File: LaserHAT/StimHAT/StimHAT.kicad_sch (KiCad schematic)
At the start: 112 parts, among them J1 GPIO, J10 OLED 0.91 (GND VCC SCL SDA), J101 ELECTRODE E1/E2, J102 B4B-PH-K-S(LF)(SN), J103 5V TO DC-DC POD, J5 GT-USB-7010ASV, J6 BNC TRIGGER IN, J7 BNC STIM OUT, Q3 AP30P30Q, Q4 DMMT5401, Q5 AP30P30Q, SW10 MSK12C02, SW6 TS-1088-AR02016, SW7 SKRHADE010, SW9 TS-1088-AR02016, U1 M24C32-WDW6TP, U101 ISO7741FDBQR, U104 TLV76050DBZR, U105 DAC60501ZDGSR, U106 OPA2192IDGKR, U107 CD74HC4053PWR, U108 DG418DY-T1-E3, U109 ISO1640BDR, U110 TLV1702AIDGKR, U4 MCP1700T-3302E/MB, U5 AP2171W, U6 CH340N, U7 MSPM0G1507SRHBR, U8 74LVC2G17GW

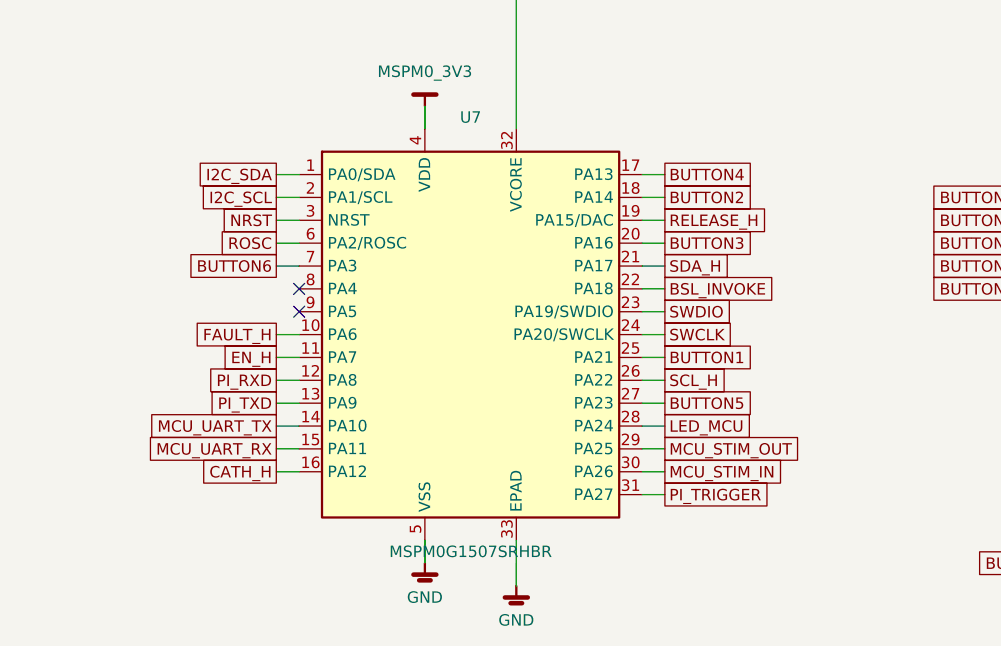
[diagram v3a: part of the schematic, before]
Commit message: StimHAT: MCU pin map re-optimised for the placement (isolator lines east on TIMA0 CCP3/CCP1/FAULT0 + ADC0 ch3/ch2, buttons and LED west/south, STIM_IN on TIMG8_CCP0); schematic, board and README updated
Co-Authored-By: Claude Fable 5.1 <noreply@anthropic.com>
Claude-Session: https://claude.ai/code/session_015kiXLxnPpBaXdXJu2EMvn7
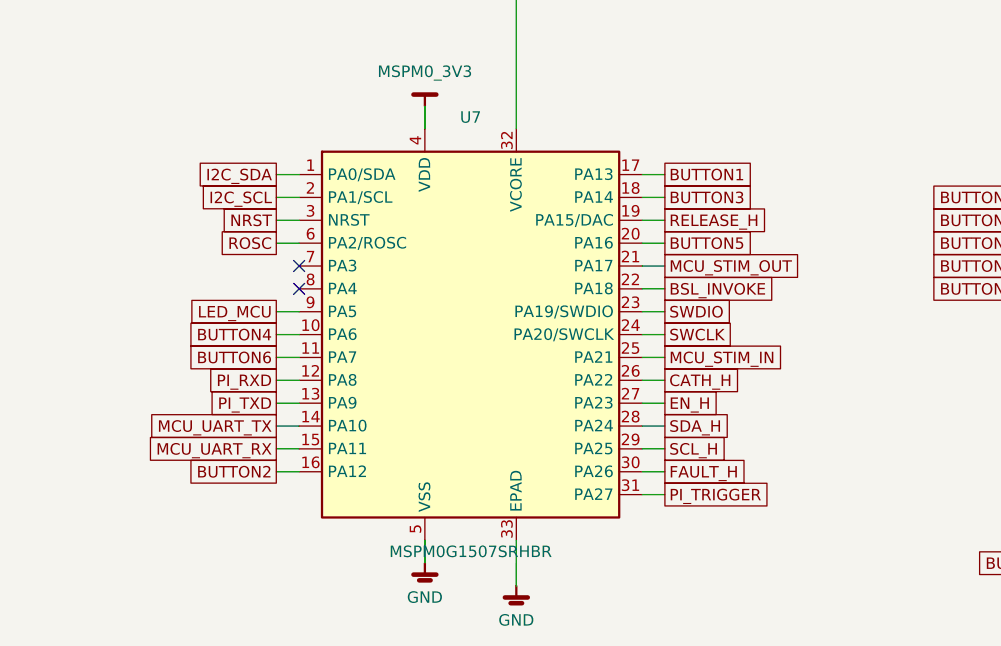
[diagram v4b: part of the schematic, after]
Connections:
- net BUTTON1: now also U7.17 (PA13); no longer U7.25 (PA21)
- net BUTTON2: now also U7.16 (PA12); no longer U7.18 (PA14)
- net BUTTON3: now also U7.18 (PA14); no longer U7.20 (PA16)
- net BUTTON4: now also U7.10 (PA6); no longer U7.17 (PA13)
- net BUTTON5: now also U7.20 (PA16); no longer U7.27 (PA23)
- net BUTTON6: now also U7.11 (PA7); no longer U7.7 (PA3)
- net CATH_H: now also U7.26 (PA22); no longer U7.16 (PA12)
- net EN_H: now also U7.27 (PA23); no longer U7.11 (PA7)
- net FAULT_H: now also U7.30 (PA26); no longer U7.10 (PA6)
- net LED_MCU: now also U7.9 (PA5); no longer U7.28 (PA24)
- net MCU_STIM_IN: now also U7.25 (PA21); no longer U7.30 (PA26)
- net MCU_STIM_OUT: now also U7.21 (PA17); no longer U7.29 (PA25)
- net SCL_H: now also U7.29 (PA25); no longer U7.26 (PA22)
- net SDA_H: now also U7.28 (PA24); no longer U7.21 (PA17)
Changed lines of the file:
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@@
   (global_label "ROSC" (shape passive) (at 364.49 71.12 180) (fields_autoplaced yes) (effects (font (size 1.27 1.27)) (justify right))
     (property "Intersheetrefs" "${INTERSHEET_REFS}" (at 364.49 71.12 0) (effects (font (size 1.27 1.27)) (hide yes))))
-  (global_label "BUTTON6" (shape passive) (at 364.49 73.66 180) (fields_autoplaced yes) (effects (font (size 1.27 1.27)) (justify right))
-    (property "Intersheetrefs" "${INTERSHEET_REFS}" (at 364.49 73.66 0) (effects (font (size 1.27 1.27)) (hide yes))))
-  (global_label "FAULT_H" (shape passive) (at 364.49 81.28 180) (fields_autoplaced yes) (effects (font (size 1.27 1.27)) (justify right))
+  (global_label "LED_MCU" (shape passive) (at 364.49 78.74 180) (fields_autoplaced yes) (effects (font (size 1.27 1.27)) (justify right))
+    (property "Intersheetrefs" "${INTERSHEET_REFS}" (at 364.49 78.74 0) (effects (font (size 1.27 1.27)) (hide yes))))
+  (global_label "BUTTON4" (shape passive) (at 364.49 81.28 180) (fields_autoplaced yes) (effects (font (size 1.27 1.27)) (justify right))
     (property "Intersheetrefs" "${INTERSHEET_REFS}" (at 364.49 81.28 0) (effects (font (size 1.27 1.27)) (hide yes))))
-  (global_label "EN_H" (shape passive) (at 364.49 83.82 180) (fields_autoplaced yes) (effects (font (size 1.27 1.27)) (justify right))
+  (global_label "BUTTON6" (shape passive) (at 364.49 83.82 180) (fields_autoplaced yes) (effects (font (size 1.27 1.27)) (justify right))
     (property "Intersheetrefs" "${INTERSHEET_REFS}" (at 364.49 83.82 0) (effects (font (size 1.27 1.27)) (hide yes))))
   (global_label "PI_RXD" (shape passive) (at 364.49 86.36 180) (fields_autoplaced yes) (effects (font (size 1.27 1.27)) (justify right))
@@
   (global_label "MCU_UART_RX" (shape passive) (at 364.49 93.98 180) (fields_autoplaced yes) (effects (font (size 1.27 1.27)) (justify right))
     (property "Intersheetrefs" "${INTERSHEET_REFS}" (at 364.49 93.98 0) (effects (font (size 1.27 1.27)) (hide yes))))
-  (global_label "CATH_H" (shape passive) (at 364.49 96.52 180) (fields_autoplaced yes) (effects (font (size 1.27 1.27)) (justify right))
+  (global_label "BUTTON2" (shape passive) (at 364.49 96.52 180) (fields_autoplaced yes) (effects (font (size 1.27 1.27)) (justify right))
     (property "Intersheetrefs" "${INTERSHEET_REFS}" (at 364.49 96.52 0) (effects (font (size 1.27 1.27)) (hide yes))))
-  (global_label "BUTTON4" (shape passive) (at 407.67 63.5 0) (fields_autoplaced yes) (effects (font (size 1.27 1.27)) (justify left))
+  (global_label "BUTTON1" (shape passive) (at 407.67 63.5 0) (fields_autoplaced yes) (effects (font (size 1.27 1.27)) (justify left))
     (property "Intersheetrefs" "${INTERSHEET_REFS}" (at 407.67 63.5 0) (effects (font (size 1.27 1.27)) (hide yes))))
-  (global_label "BUTTON2" (shape passive) (at 407.67 66.04 0) (fields_autoplaced yes) (effects (font (size 1.27 1.27)) (justify left))
+  (global_label "BUTTON3" (shape passive) (at 407.67 66.04 0) (fields_autoplaced yes) (effects (font (size 1.27 1.27)) (justify left))
     (property "Intersheetrefs" "${INTERSHEET_REFS}" (at 407.67 66.04 0) (effects (font (size 1.27 1.27)) (hide yes))))
   (global_label "RELEASE_H" (shape passive) (at 407.67 68.58 0) (fields_autoplaced yes) (effects (font (size 1.27 1.27)) (justify left))
     (property "Intersheetrefs" "${INTERSHEET_REFS}" (at 407.67 68.58 0) (effects (font (size 1.27 1.27)) (hide yes))))
-  (global_label "BUTTON3" (shape passive) (at 407.67 71.12 0) (fields_autoplaced yes) (effects (font (size 1.27 1.27)) (justify left))
+  (global_label "BUTTON5" (shape passive) (at 407.67 71.12 0) (fields_autoplaced yes) (effects (font (size 1.27 1.27)) (justify left))
     (property "Intersheetrefs" "${INTERSHEET_REFS}" (at 407.67 71.12 0) (effects (font (size 1.27 1.27)) (hide yes))))
-  (global_label "SDA_H" (shape passive) (at 407.67 73.66 0) (fields_autoplaced yes) (effects (font (size 1.27 1.27)) (justify left))
+  (global_label "MCU_STIM_OUT" (shape passive) (at 407.67 73.66 0) (fields_autoplaced yes) (effects (font (size 1.27 1.27)) (justify left))
     (property "Intersheetrefs" "${INTERSHEET_REFS}" (at 407.67 73.66 0) (effects (font (size 1.27 1.27)) (hide yes))))
   (global_label "BSL_INVOKE" (shape passive) (at 407.67 76.2 0) (fields_autoplaced yes) (effects (font (size 1.27 1.27)) (justify left))
@@
   (global_label "SWCLK" (shape passive) (at 407.67 81.28 0) (fields_autoplaced yes) (effects (font (size 1.27 1.27)) (justify left))
     (property "Intersheetrefs" "${INTERSHEET_REFS}" (at 407.67 81.28 0) (effects (font (size 1.27 1.27)) (hide yes))))
-  (global_label "BUTTON1" (shape passive) (at 407.67 83.82 0) (fields_autoplaced yes) (effects (font (size 1.27 1.27)) (justify left))
+  (global_label "MCU_STIM_IN" (shape passive) (at 407.67 83.82 0) (fields_autoplaced yes) (effects (font (size 1.27 1.27)) (justify left))
     (property "Intersheetrefs" "${INTERSHEET_REFS}" (at 407.67 83.82 0) (effects (font (size 1.27 1.27)) (hide yes))))
-  (global_label "SCL_H" (shape passive) (at 407.67 86.36 0) (fields_autoplaced yes) (effects (font (size 1.27 1.27)) (justify left))
+  (global_label "CATH_H" (shape passive) (at 407.67 86.36 0) (fields_autoplaced yes) (effects (font (size 1.27 1.27)) (justify left))
     (property "Intersheetrefs" "${INTERSHEET_REFS}" (at 407.67 86.36 0) (effects (font (size 1.27 1.27)) (hide yes))))
-  (global_label "BUTTON5" (shape passive) (at 407.67 88.9 0) (fields_autoplaced yes) (effects (font (size 1.27 1.27)) (justify left))
+  (global_label "EN_H" (shape passive) (at 407.67 88.9 0) (fields_autoplaced yes) (effects (font (size 1.27 1.27)) (justify left))
     (property "Intersheetrefs" "${INTERSHEET_REFS}" (at 407.67 88.9 0) (effects (font (size 1.27 1.27)) (hide yes))))
-  (global_label "LED_MCU" (shape passive) (at 407.67 91.44 0) (fields_autoplaced yes) (effects (font (size 1.27 1.27)) (justify left))
+  (global_label "SDA_H" (shape passive) (at 407.67 91.44 0) (fields_autoplaced yes) (effects (font (size 1.27 1.27)) (justify left))
     (property "Intersheetrefs" "${INTERSHEET_REFS}" (at 407.67 91.44 0) (effects (font (size 1.27 1.27)) (hide yes))))
-  (global_label "MCU_STIM_OUT" (shape passive) (at 407.67 93.98 0) (fields_autoplaced yes) (effects (font (size 1.27 1.27)) (justify left))
+  (global_label "SCL_H" (shape passive) (at 407.67 93.98 0) (fields_autoplaced yes) (effects (font (size 1.27 1.27)) (justify left))
     (property "Intersheetrefs" "${INTERSHEET_REFS}" (at 407.67 93.98 0) (effects (font (size 1.27 1.27)) (hide yes))))
-  (global_label "MCU_STIM_IN" (shape passive) (at 407.67 96.52 0) (fields_autoplaced yes) (effects (font (size 1.27 1.27)) (justify left))
+  (global_label "FAULT_H" (shape passive) (at 407.67 96.52 0) (fields_autoplaced yes) (effects (font (size 1.27 1.27)) (justify left))
     (property "Intersheetrefs" "${INTERSHEET_REFS}" (at 407.67 96.52 0) (effects (font (size 1.27 1.27)) (hide yes))))
   (global_label "PI_TRIGGER" (shape passive) (at 407.67 99.06 0) (fields_autoplaced yes) (effects (font (size 1.27 1.27)) (justify left))
@@
   (no_connect (at 208.28 139.7))
   (no_connect (at 208.28 142.24))
+  (no_connect (at 367.03 73.66))
   (no_connect (at 367.03 76.2))
-  (no_connect (at 367.03 78.74))
   (no_connect (at 50.8 335.28))
   (no_connect (at 71.12 335.28))
@@
   (wire (pts (xy 364.49 68.58) (xy 367.03 68.58)) (stroke (width 0) (type default)))
   (wire (pts (xy 364.49 71.12) (xy 367.03 71.12)) (stroke (width 0) (type default)))
-  (wire (pts (xy 364.49 73.66) (xy 367.03 73.66)) (stroke (width 0) (type default)))
+  (wire (pts (xy 364.49 78.74) (xy 367.03 78.74)) (stroke (width 0) (type default)))
   (wire (pts (xy 364.49 81.28) (xy 367.03 81.28)) (stroke (width 0) (type default)))
   (wire (pts (xy 364.49 83.82) (xy 367.03 83.82)) (stroke (width 0) (type default)))

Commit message: StimHAT: PI_TRIGGER moved to Pi GPIO10 (J1.19) / U7 pin 8, RELEASE_H to pin 31
At the user's request (routing): the trigger line now comes straight down from the header's west
half into PA4 (pin 8) instead of crossing the board from J1.37 to PA27; RELEASE_H takes pin 31
(PA27) so it leaves U7 on the isolator side; pin 19 (PA15, DAC0_OUT) and pin 7 (PA3) are spare.
GPIO10 rather than 4 / 17 / 22 / 27 (bonnet buttons) or 7 / 8 (pull up at boot).

Schematic regenerated (netcheck OK, ERC 0), nets pushed into the board with the tracks kept
(path / sync checks 0), placement table synced from the user's board (21 parts).  README pin map
updated.  The Pi software still defaults to GPIO 26: StimHAT needs LASERHAT_TRIGGER_PIN=10 and
`laserhat-brokerd --gpio-pin 10`.

Co-Authored-By: Claude Fable 5.1 <noreply@anthropic.com>
Claude-Session: https://claude.ai/code/session_015kiXLxnPpBaXdXJu2EMvn7
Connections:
- net PI_TRIGGER: now also J1.19 (GPIO10), U7.8 (PA4); no longer J1.37 (GPIO26), U7.31 (PA27)
- net RELEASE_H: now also U7.31 (PA27); no longer U7.19 (PA15/DAC)
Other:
- note added: "Module lines from the Rev 2 J8 / J9 pins: PA6 FAULT_H, PA7 EN_H, PA12 CATH_H, PA15 RELEASE_H, PA17 SDA_H, PA22 SCL_H (StimHAT: see the README's pin map). Joystick SW7 (SKRHADE010): up PA13,"
- note removed: "Module lines from the Rev 2 J8 / J9 pins: PA6 FAULT_H, PA7 EN_H, PA12 CATH_H, PA15 RELEASE_H, PA17 SDA_H, PA22 SCL_H. Joystick SW7 (SKRHADE010): up PA13,"
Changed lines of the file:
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@@
   (global_label "I2C_SCL" (shape passive) (at 33.02 66.04 180) (fields_autoplaced yes) (effects (font (size 1.27 1.27)) (justify right))
     (property "Intersheetrefs" "${INTERSHEET_REFS}" (at 33.02 66.04 0) (effects (font (size 1.27 1.27)) (hide yes))))
+  (global_label "PI_TRIGGER" (shape passive) (at 33.02 83.82 180) (fields_autoplaced yes) (effects (font (size 1.27 1.27)) (justify right))
+    (property "Intersheetrefs" "${INTERSHEET_REFS}" (at 33.02 83.82 0) (effects (font (size 1.27 1.27)) (hide yes))))
   (global_label "ID_SDA" (shape passive) (at 33.02 93.98 180) (fields_autoplaced yes) (effects (font (size 1.27 1.27)) (justify right))
     (property "Intersheetrefs" "${INTERSHEET_REFS}" (at 33.02 93.98 0) (effects (font (size 1.27 1.27)) (hide yes))))
-  (global_label "PI_TRIGGER" (shape passive) (at 33.02 106.68 180) (fields_autoplaced yes) (effects (font (size 1.27 1.27)) (justify right))
-    (property "Intersheetrefs" "${INTERSHEET_REFS}" (at 33.02 106.68 0) (effects (font (size 1.27 1.27)) (hide yes))))
   (global_label "PI_TXD" (shape passive) (at 68.58 68.58 0) (fields_autoplaced yes) (effects (font (size 1.27 1.27)) (justify left))
     (property "Intersheetrefs" "${INTERSHEET_REFS}" (at 68.58 68.58 0) (effects (font (size 1.27 1.27)) (hide yes))))
@@
   (global_label "ROSC" (shape passive) (at 364.49 71.12 180) (fields_autoplaced yes) (effects (font (size 1.27 1.27)) (justify right))
     (property "Intersheetrefs" "${INTERSHEET_REFS}" (at 364.49 71.12 0) (effects (font (size 1.27 1.27)) (hide yes))))
+  (global_label "PI_TRIGGER" (shape passive) (at 364.49 76.2 180) (fields_autoplaced yes) (effects (font (size 1.27 1.27)) (justify right))
+    (property "Intersheetrefs" "${INTERSHEET_REFS}" (at 364.49 76.2 0) (effects (font (size 1.27 1.27)) (hide yes))))
   (global_label "LED_MCU" (shape passive) (at 364.49 78.74 180) (fields_autoplaced yes) (effects (font (size 1.27 1.27)) (justify right))
     (property "Intersheetrefs" "${INTERSHEET_REFS}" (at 364.49 78.74 0) (effects (font (size 1.27 1.27)) (hide yes))))
@@
   (global_label "BUTTON3" (shape passive) (at 407.67 66.04 0) (fields_autoplaced yes) (effects (font (size 1.27 1.27)) (justify left))
     (property "Intersheetrefs" "${INTERSHEET_REFS}" (at 407.67 66.04 0) (effects (font (size 1.27 1.27)) (hide yes))))
-  (global_label "RELEASE_H" (shape passive) (at 407.67 68.58 0) (fields_autoplaced yes) (effects (font (size 1.27 1.27)) (justify left))
-    (property "Intersheetrefs" "${INTERSHEET_REFS}" (at 407.67 68.58 0) (effects (font (size 1.27 1.27)) (hide yes))))
   (global_label "BUTTON5" (shape passive) (at 407.67 71.12 0) (fields_autoplaced yes) (effects (font (size 1.27 1.27)) (justify left))
     (property "Intersheetrefs" "${INTERSHEET_REFS}" (at 407.67 71.12 0) (effects (font (size 1.27 1.27)) (hide yes))))
@@
   (global_label "FAULT_H" (shape passive) (at 407.67 96.52 0) (fields_autoplaced yes) (effects (font (size 1.27 1.27)) (justify left))
     (property "Intersheetrefs" "${INTERSHEET_REFS}" (at 407.67 96.52 0) (effects (font (size 1.27 1.27)) (hide yes))))
-  (global_label "PI_TRIGGER" (shape passive) (at 407.67 99.06 0) (fields_autoplaced yes) (effects (font (size 1.27 1.27)) (justify left))
+  (global_label "RELEASE_H" (shape passive) (at 407.67 99.06 0) (fields_autoplaced yes) (effects (font (size 1.27 1.27)) (justify left))
     (property "Intersheetrefs" "${INTERSHEET_REFS}" (at 407.67 99.06 0) (effects (font (size 1.27 1.27)) (hide yes))))
   (symbol (lib_id "stimhat:R") (at 274.32 101.6 0) (unit 1) (exclude_from_sim no) (in_bom yes) (on_board yes) (dnp no)
@@
   (global_label "I2C_SDA" (shape passive) (at 478.79 140.97 0) (fields_autoplaced yes) (effects (font (size 1.27 1.27)) (justify left))
     (property "Intersheetrefs" "${INTERSHEET_REFS}" (at 478.79 140.97 0) (effects (font (size 1.27 1.27)) (hide yes))))
-  (text "Module lines from the Rev 2 J8 / J9 pins: PA6 FAULT_H, PA7 EN_H, PA12 CATH_H, PA15 RELEASE_H, PA17 SDA_H, PA22 SCL_H.  Joystick SW7 (SKRHADE010): up PA13," (exclude_from_sim no) (at 261.62 144.78 0) (effects (font (size 1.27 1.27)) (justify left bottom)))
+  (text "Module lines from the Rev 2 J8 / J9 pins: PA6 FAULT_H, PA7 EN_H, PA12 CATH_H, PA15 RELEASE_H, PA17 SDA_H, PA22 SCL_H (StimHAT: see the README's pin map).  Joystick SW7 (SKRHADE010): up PA13," (exclude_from_sim no) (at 261.62 144.78 0) (effects (font (size 1.27 1.27)) (justify left bottom)))
   (text "down PA16, centre PA14, left PA21 (BACK), right PA3 (BUTTON6, new); FIRE SW9 PA23; all active low.  J10: unpopulated socket for a 0.91 in I2C OLED instead of the bonnet." (exclude_from_sim no) (at 261.62 149.86 0) (effects (font (size 1.27 1.27)) (justify left bottom)))
   (rectangle (start 513.08 20.32) (end 640.08 101.6) (stroke (width 0.2) (type dash)) (fill (type none)))
@@
   (no_connect (at 38.1 78.74))
   (no_connect (at 63.5 78.74))
-  (no_connect (at 38.1 83.82))
   (no_connect (at 38.1 86.36))
   (no_connect (at 38.1 88.9))
@@
   (no_connect (at 38.1 101.6))
   (no_connect (at 38.1 104.14))
+  (no_connect (at 38.1 106.68))
   (no_connect (at 63.5 106.68))
   (no_connect (at 63.5 109.22))
@@
   (no_connect (at 208.28 142.24))
   (no_connect (at 367.03 73.66))
-  (no_connect (at 367.03 76.2))
+  (no_connect (at 405.13 68.58))
   (no_connect (at 50.8 335.28))
   (no_connect (at 71.12 335.28))
@@
   (wire (pts (xy 33.02 63.5) (xy 38.1 63.5)) (stroke (width 0) (type default)))
   (wire (pts (xy 33.02 66.04) (xy 38.1 66.04)) (stroke (width 0) (type default)))
+  (wire (pts (xy 33.02 83.82) (xy 38.1 83.82)) (stroke (width 0) (type default)))
   (wire (pts (xy 33.02 93.98) (xy 38.1 93.98)) (stroke (width 0) (type default)))
-  (wire (pts (xy 33.02 106.68) (xy 38.1 106.68)) (stroke (width 0) (type default)))
   (wire (pts (xy 63.5 68.58) (xy 68.58 68.58)) (stroke (width 0) (type default)))
   (wire (pts (xy 63.5 71.12) (xy 68.58 71.12)) (stroke (width 0) (type default)))
@@
   (wire (pts (xy 364.49 68.58) (xy 367.03 68.58)) (stroke (width 0) (type default)))
   (wire (pts (xy 364.49 71.12) (xy 367.03 71.12)) (stroke (width 0) (type default)))
+  (wire (pts (xy 364.49 76.2) (xy 367.03 76.2)) (stroke (width 0) (type default)))
   (wire (pts (xy 364.49 78.74) (xy 367.03 78.74)) (stroke (width 0) (type default)))
   (wire (pts (xy 364.49 81.28) (xy 367.03 81.28)) (stroke (width 0) (type default)))
@@
   (wire (pts (xy 405.13 63.5) (xy 407.67 63.5)) (stroke (width 0) (type default)))
   (wire (pts (xy 405.13 66.04) (xy 407.67 66.04)) (stroke (width 0) (type default)))
-  (wire (pts (xy 405.13 68.58) (xy 407.67 68.58)) (stroke (width 0) (type default)))
   (wire (pts (xy 405.13 71.12) (xy 407.67 71.12)) (stroke (width 0) (type default)))
   (wire (pts (xy 405.13 73.66) (xy 407.67 73.66)) (stroke (width 0) (type default)))
